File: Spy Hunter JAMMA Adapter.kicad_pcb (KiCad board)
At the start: 2 copper layers, 111.4 x 135.4 mm, 92 parts, among them P1 1K, P2 1K, P3 10K, P4 1K, SW2 SW_DIP_SPSTx02_Slide_9.78x7.2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, U1 74LS86, U10 NE555, U11 LM386, U12 CD4099B, U2 74LS74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

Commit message: update BOM and snapshots
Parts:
- CSDJ1: renamed from CSQD - J1
- renumbered MCRJ1 to CSDJ2, CSQDJ3 to CSDJ3
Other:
- board text added: "CSD J1 - DATA"
- board text added: "CSD J3 - MUSIC"
- board text removed: "J1 - DATA"
- board text removed: "J3 - MUSIC"
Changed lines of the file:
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@@
 		(descr "Through hole straight pin header, 1x06, 2.54mm pitch, single row")
 		(tags "Through hole pin header THT 1x06 2.54mm single row")
-		(property "Reference" "CSQDJ3"
+		(property "Reference" "CSDJ3"
 			(at 0 -2.38 0)
 			(layer "F.SilkS")
@@
 		(descr "Molex KK 396 Interconnect System, old/engineering part number: 5273-05A example for new part number: 09-65-2058, 5 Pins (https://www.molex.com/pdm_docs/sd/009652028_sd.pdf), generated with kicad-footprint-generator")
 		(tags "connector Molex KK-396 vertical")
-		(property "Reference" "MCRJ1"
+		(property "Reference" "CSDJ2"
 			(at 7.92 -6.8 90)
 			(layer "F.SilkS")
@@
 		(descr "Through hole straight pin header, 1x05, 2.54mm pitch, single row")
 		(tags "Through hole pin header THT 1x05 2.54mm single row")
-		(property "Reference" "CSQD - J1"
+		(property "Reference" "CSDJ1"
 			(at 0 -2.38 180)
 			(layer "F.SilkS" knockout)
@@
 		)
 	)
-	(gr_text "J1 - DATA"
+	(gr_text "CSD J1 - DATA"
 		(at 154.6 144.88 90)
 		(layer "F.SilkS")
@@
 		)
 	)
-	(gr_text "J3 - MUSIC"
+	(gr_text "CSD J3 - MUSIC"
 		(at 154.608358 128.75 90)
 		(layer "F.SilkS")

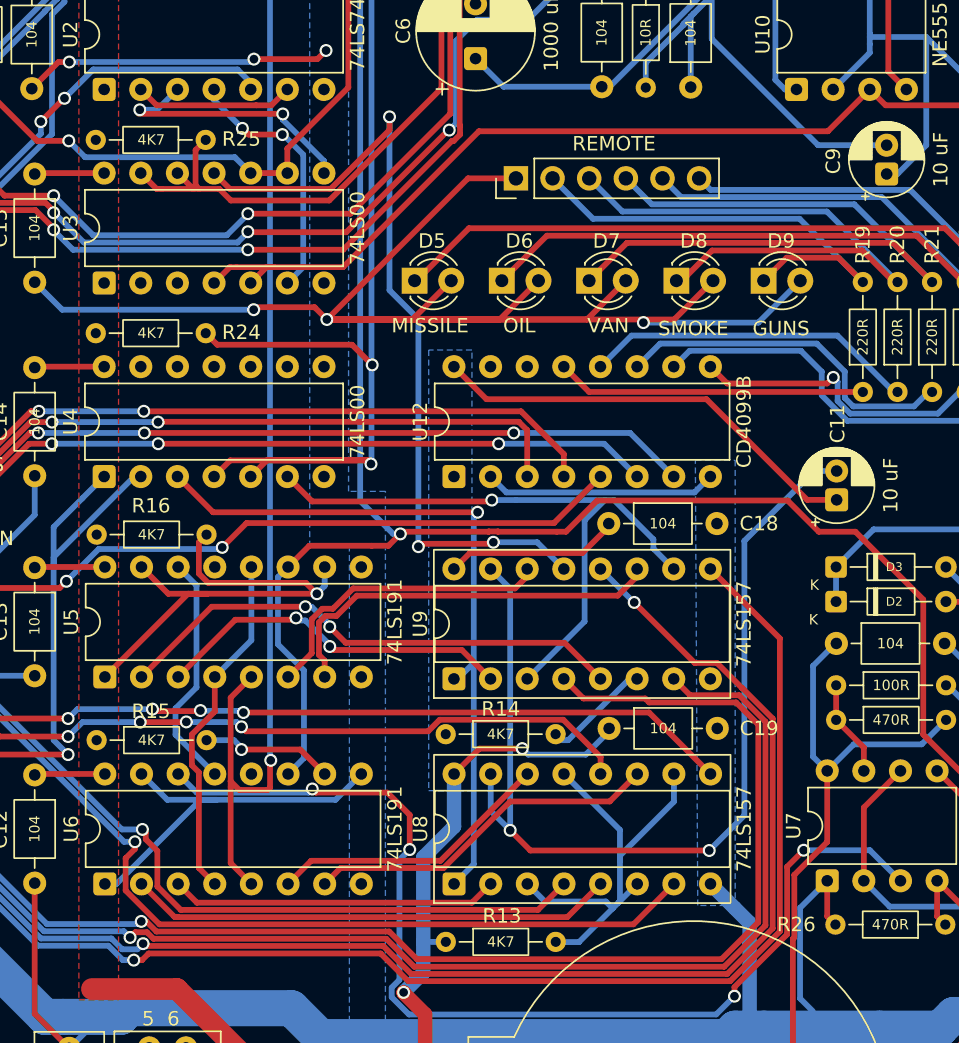
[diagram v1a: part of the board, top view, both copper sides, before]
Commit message: get rid of unnecessary pull-ups
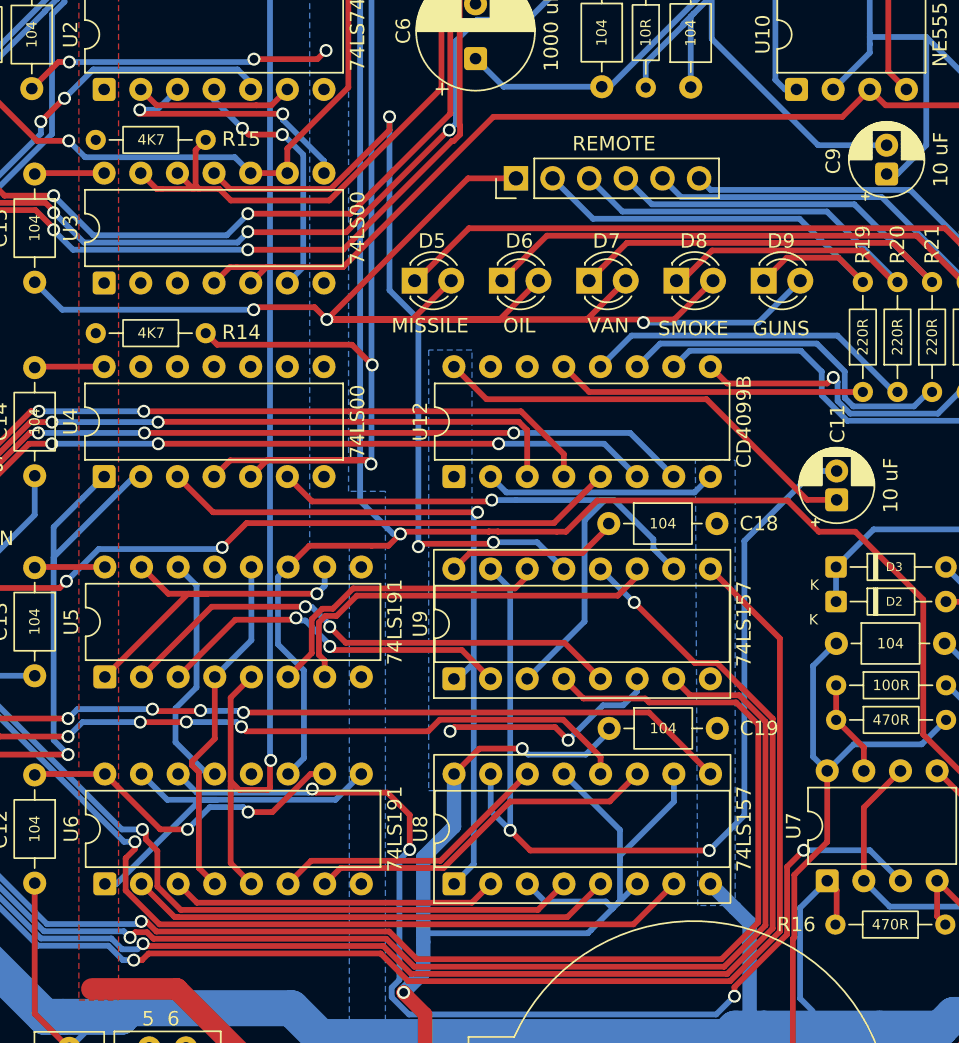
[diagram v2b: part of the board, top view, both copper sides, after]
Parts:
- removed R13: 4K7, Resistor_THT:R_Axial_DIN0204_L3.6mm_D1.6mm_P7.62mm_Horizontal
- removed the R14 at (101.5, 120.8)
- removed the R15 at (77.3, 121.2)
- removed the R16 at (77.3, 107.0)
- renumbered R24 to R14, R25 to R15, R26 to R16
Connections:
- U5 pad 1: +5V_R16 -> +5V
- U5 pad 10: +5V_R16 -> +5V
- U5 pad 15: +5V_R16 -> +5V
- U6 pad 10: +5V_R15 -> +5V
- U8 pad 10: +5V_R13 -> +5V
- U8 pad 13: +5V_R13 -> +5V
- U8 pad 3: +5V_R13 -> +5V
- U8 pad 6: +5V_R13 -> +5V
- U9 pad 6: +5V_R14 -> +5V
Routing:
- net +5V: track 529.4 -> 627.8 mm, vias 8 -> 13
- net +5V_R16: track 36.2 -> 0.00 mm, vias 1 -> 0
- net +5V_R13: track 32.1 -> 0.00 mm
- net +5V_R15: track 8.92 -> 0.00 mm, vias 1 -> 0
- net +5V_R14: track 7.58 -> 0.00 mm

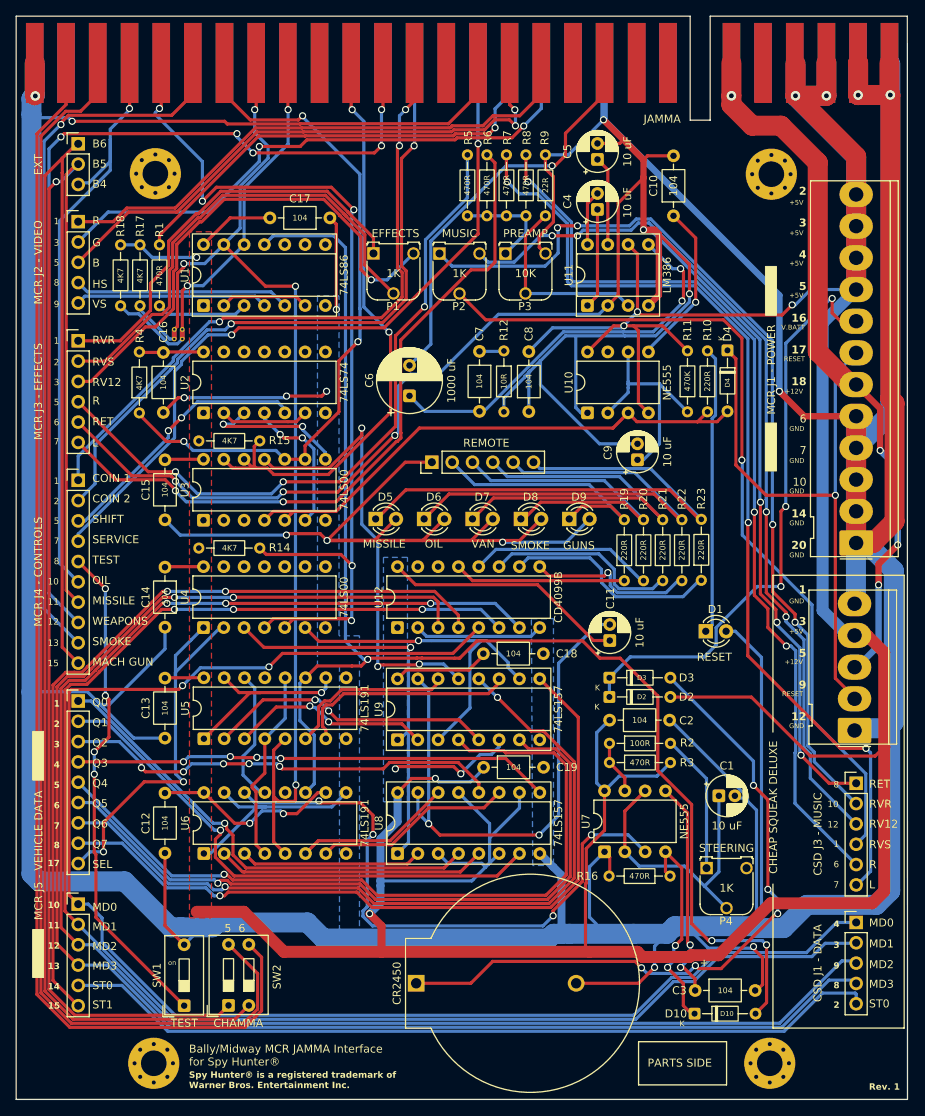
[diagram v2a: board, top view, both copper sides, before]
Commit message: reposition kick harness connector
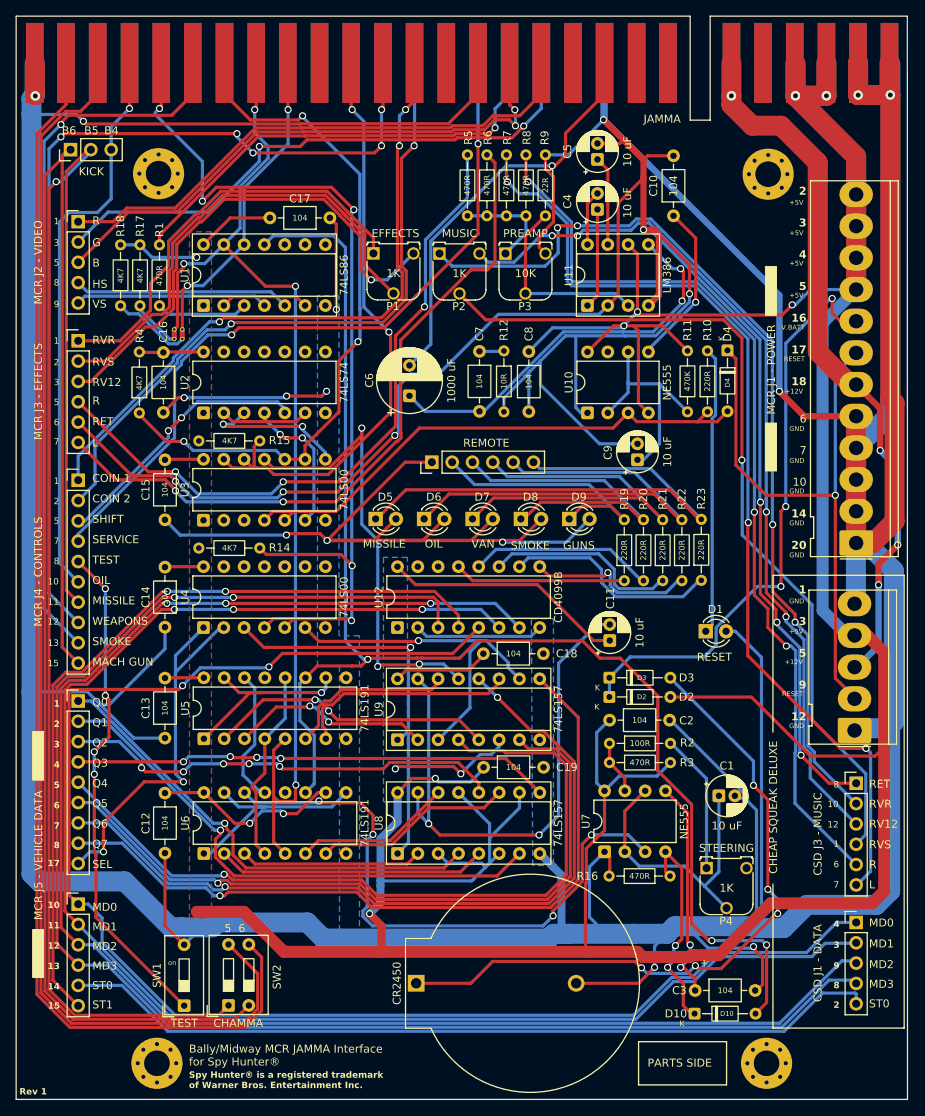
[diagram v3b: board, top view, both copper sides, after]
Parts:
- moved KICK 1.21 mm to (61.2, 43.2), turned to 90 degrees
- moved PMH1 0.40 mm to (72.2, 46.2)
- moved PMH2 0.40 mm to (148.2, 157.4)
- moved PMH3 0.40 mm to (72.0, 157.4)
- moved PMH4 0.40 mm to (148.4, 46.3)
- renumbered EXT to KICK
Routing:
- net 1P_B4: track 77.3 -> 71.7 mm
- net 1P_B5: track 185.5 -> 190.4 mm
- net 1P_B6: track 199.4 -> 198.3 mm
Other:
- board text added: "Rev 1"
- board text removed: "Rev. 1"

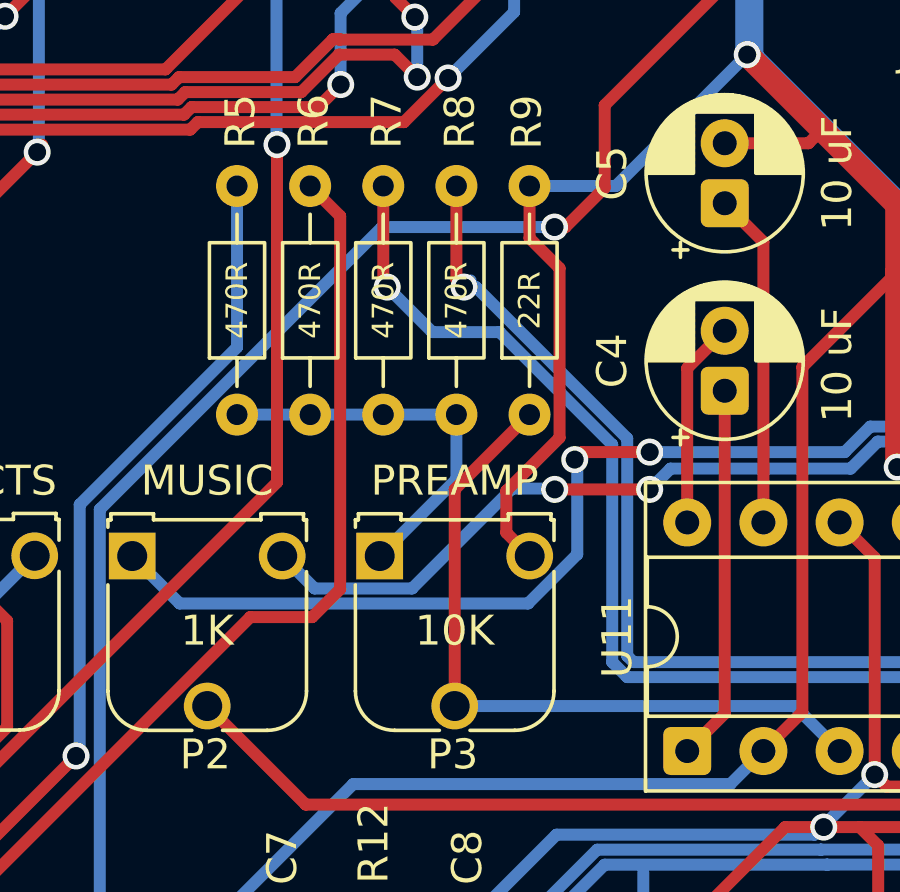
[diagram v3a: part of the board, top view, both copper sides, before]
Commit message: swap initial/final pins of P3
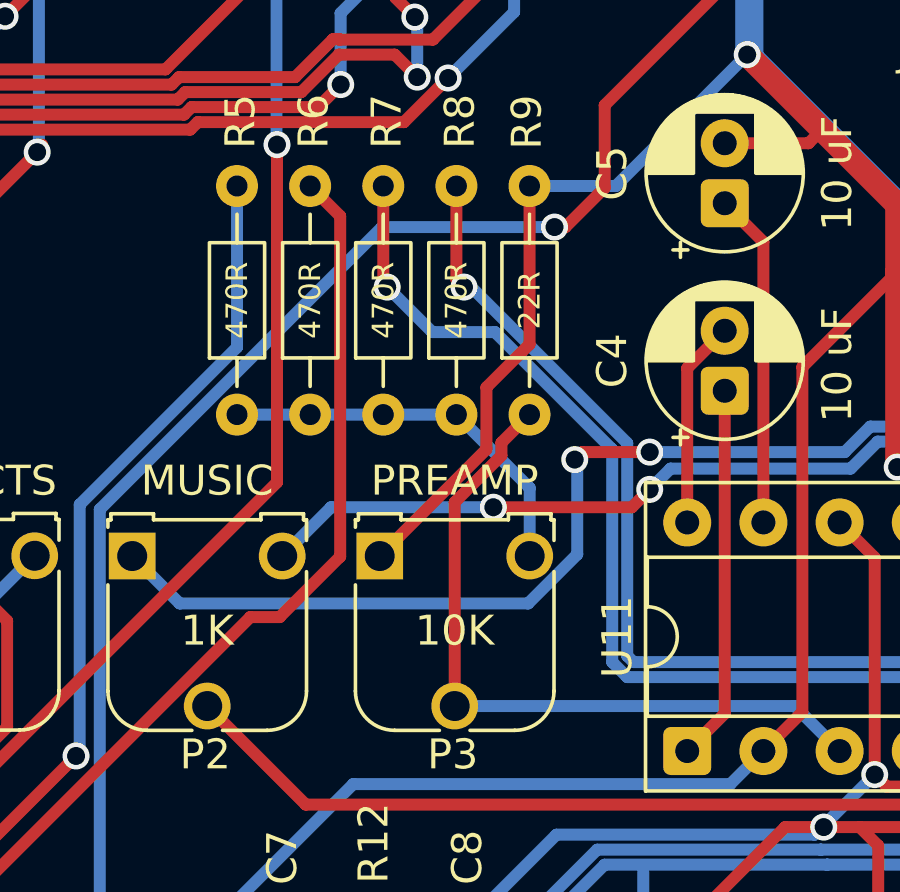
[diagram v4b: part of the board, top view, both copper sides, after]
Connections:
- P3 pad 1: AUDIO_MONO -> GND
- P3 pad 3: GND -> AUDIO_MONO
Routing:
- net MUSIC_RV12: track 109.6 -> 108.7 mm
- net EFFECTS_L: track 88.7 -> 88.1 mm
- net GND: track 1352.3 -> 1352.9 mm

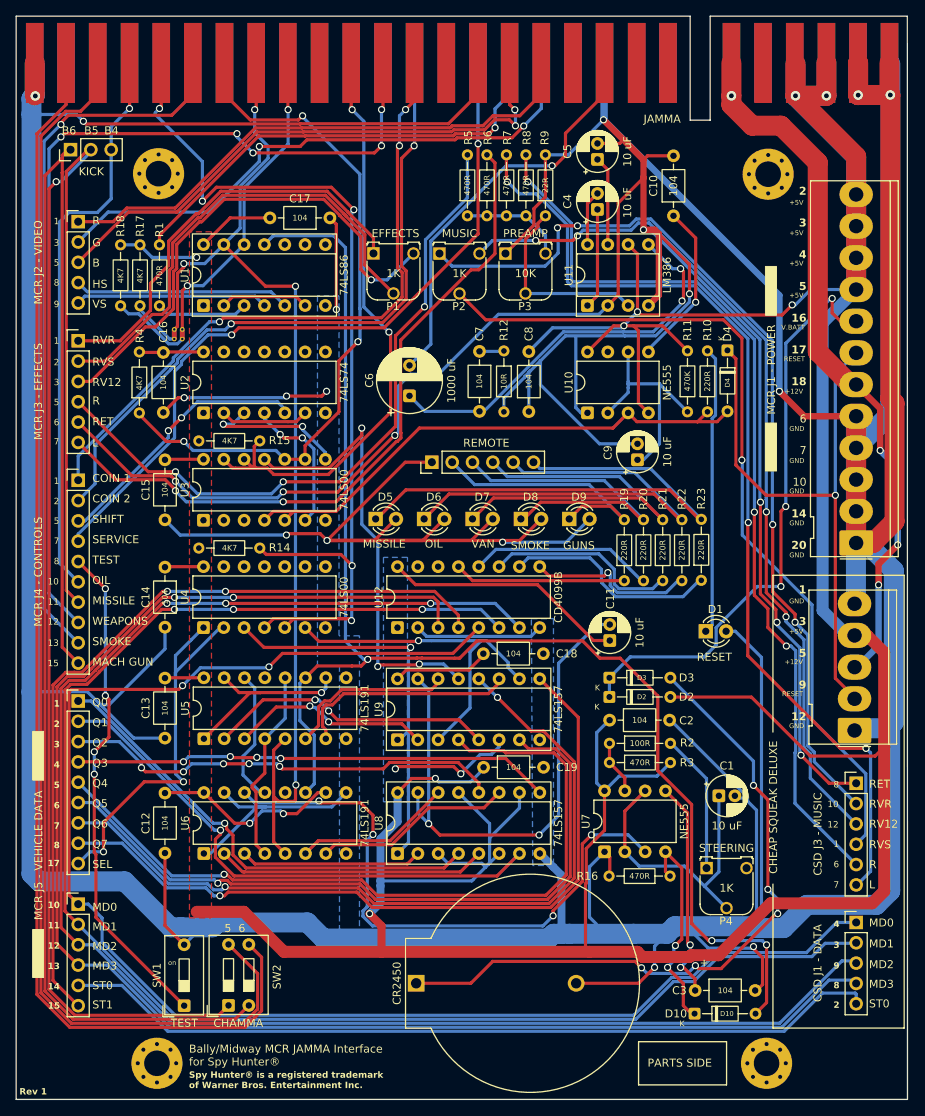
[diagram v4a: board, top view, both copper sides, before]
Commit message: trace cleanup
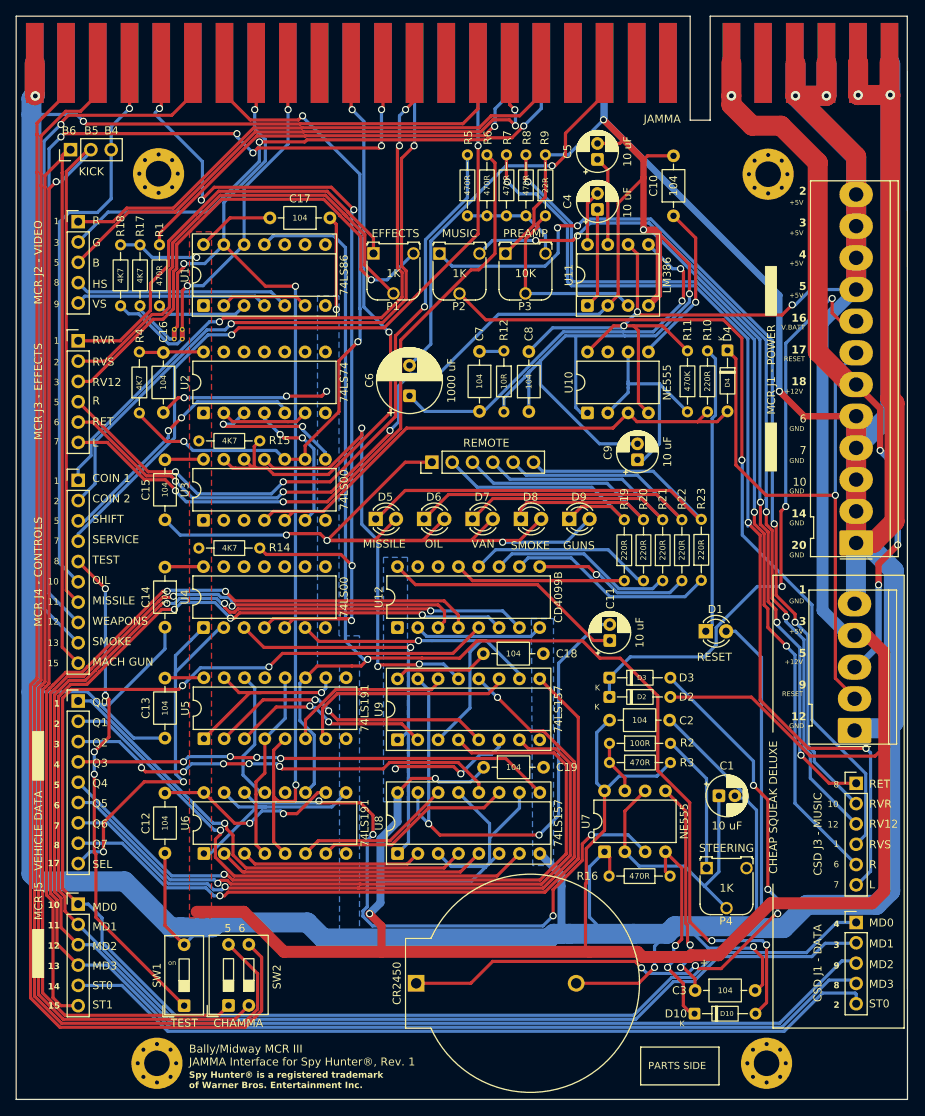
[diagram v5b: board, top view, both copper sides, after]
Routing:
- net Q4: track 96.6 -> 93.4 mm
- net Q5: track 89.7 -> 86.6 mm
- net Q7: track 94.8 -> 91.6 mm
- net Q6: track 98.6 -> 95.5 mm
- net MUSIC_L: track 123.5 -> 125.9 mm
- net U12_DISABLE: track 99.7 -> 101.7 mm
- net U12_A1: track 195.5 -> 197.4 mm
- net U12_DATA: track 194.7 -> 196.6 mm
- net U12_A2: track 200.6 -> 202.3 mm
- net 1P_B5_CHAMMA: track 159.2 -> 160.6 mm
- net 1P_B6: track 198.3 -> 199.7 mm
- net 1P_B5: track 190.4 -> 191.8 mm
- net 1P_B6_CHAMMA: track 157.5 -> 158.9 mm
- net U12_Q0: track 20.9 -> 19.7 mm
- net U12_Q2: track 24.4 -> 23.3 mm
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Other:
- board text added: "Bally/Midway MCR III JAMMA Interface for Spy Hunter®, Rev. 1"
- board text removed: "Bally/Midway MCR JAMMA Interface for Spy Hunter®"
- board text removed: "Rev 1"
